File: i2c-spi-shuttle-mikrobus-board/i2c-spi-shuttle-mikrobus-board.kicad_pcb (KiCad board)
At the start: 4 copper layers, 25.4 x 42.9 mm, 14 parts, among them J1 Conn_01x08, J2 Conn_01x08, J3 Shuttle, SW1 ADDR, U1 SC18IS606PW, U2 PCAL9538APW

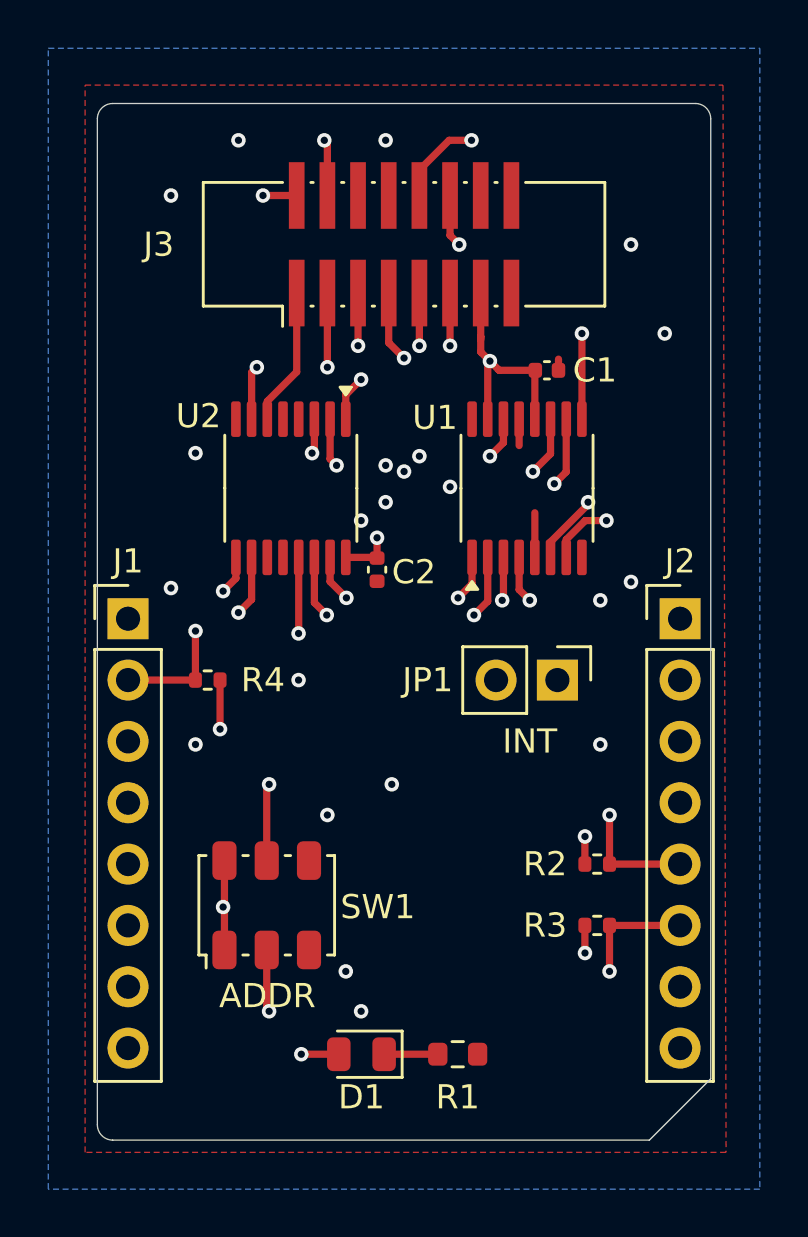
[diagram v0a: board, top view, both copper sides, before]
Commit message: fix shuttle pinout in schematic, clear PCB of tracks (we must reroute)
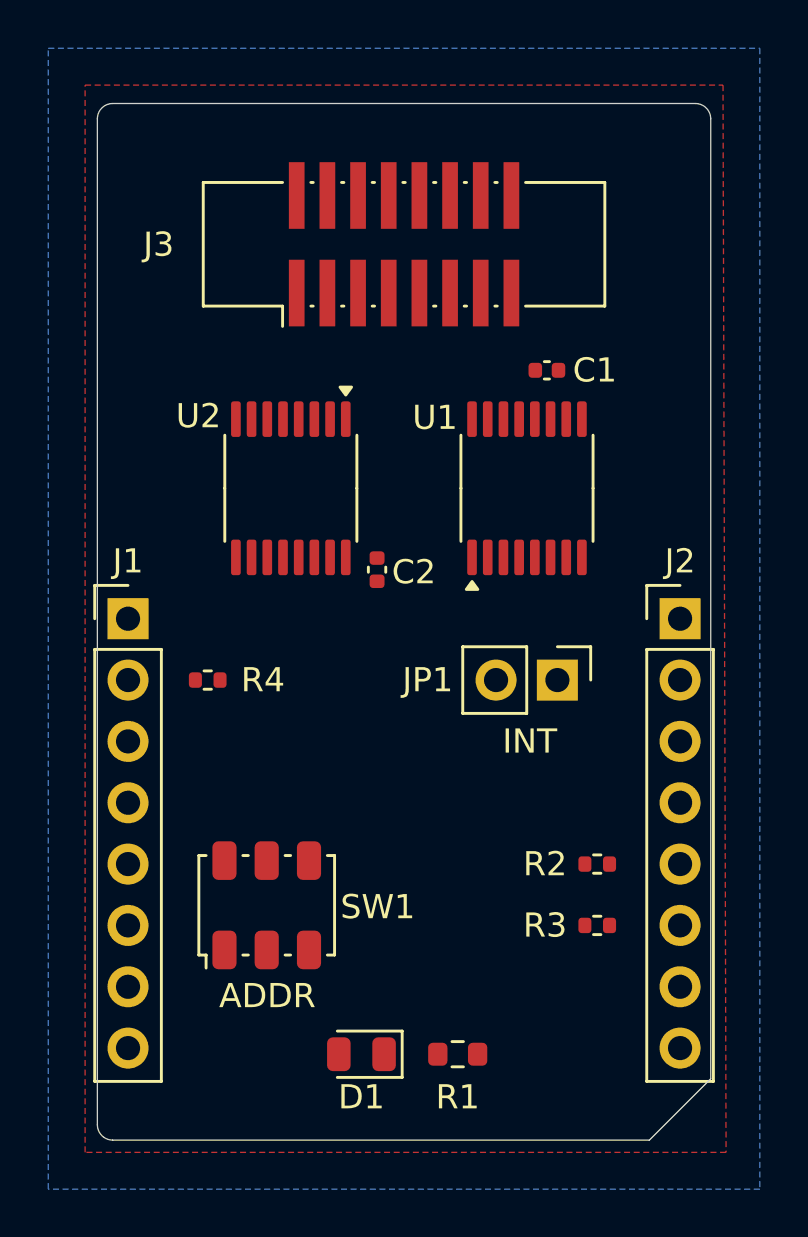
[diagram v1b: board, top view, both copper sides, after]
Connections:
- J3 pad 1: /OUT_AN -> /GND
- J3 pad 10: /SCL -> /OUT_SCK
- J3 pad 11: /OUT_COPI -> /OUT_RX
- J3 pad 12: /SDA -> /OUT_~{CS}
- J3 pad 13: /+3.3V -> /OUT_~{INT}
- J3 pad 14: /OUT_+5V -> /OUT_~{RST}
- J3 pad 15: /GND -> /OUT_PWM
- J3 pad 16: /GND -> /OUT_AN
- J3 pad 2: /OUT_PWM -> /GND
- J3 pad 3: /OUT_~{RST} -> /OUT_+5V
- J3 pad 4: /OUT_~{INT} -> /+3.3V
- J3 pad 5: /OUT_~{CS} -> /SDA
- J3 pad 6: /OUT_RX -> /OUT_COPI
- J3 pad 7: /OUT_SCK -> /SCL
- J3 pad 8: /OUT_TX -> /OUT_CIPO
- J3 pad 9: /OUT_CIPO -> /OUT_TX
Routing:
- net /SDA: track 70.4 -> 0.00 mm, vias 7 -> 0
- net /SCL: track 59.7 -> 0.00 mm, vias 5 -> 0
- net /IN_~{RST}: track 50.8 -> 0.00 mm, vias 7 -> 0
- net /A0: track 47.3 -> 0.00 mm, vias 5 -> 0
- net /A1: track 37.0 -> 0.00 mm, vias 6 -> 0
- net /OUT_~{INT}: track 28.0 -> 0.00 mm, vias 3 -> 0
- net /OUT_PWM: track 25.3 -> 0.00 mm, vias 4 -> 0
- net /+3.3V: track 22.4 -> 0.00 mm, vias 7 -> 0
- net /MID_~{INT}: track 18.5 -> 0.00 mm, vias 3 -> 0
- net /OUT_SCK: track 15.5 -> 0.00 mm, vias 3 -> 0
- net /OUT_COPI: track 15.3 -> 0.00 mm, vias 3 -> 0
- net /OUT_~{CS}: track 15.2 -> 0.00 mm, vias 2 -> 0
- net /OUT_CIPO: track 11.4 -> 0.00 mm, vias 3 -> 0
- net /OUT_~{RST}: track 8.23 -> 0.00 mm, vias 2 -> 0
- net /OUT_AN: track 5.73 -> 0.00 mm
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
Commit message: route the I2C-SPI Shuttle board now that the pinout is fixed
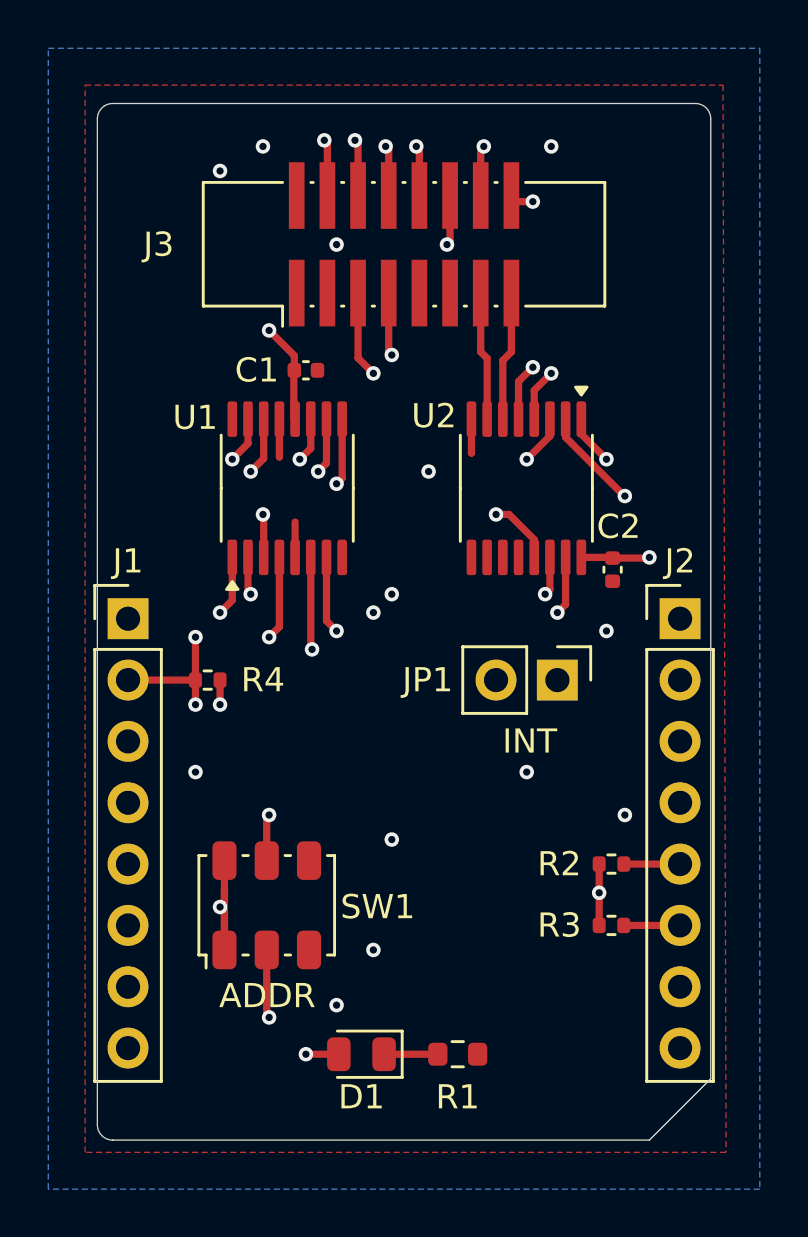
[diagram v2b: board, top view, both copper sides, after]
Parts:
- moved C1 9.98 mm to (84.8, 46.9)
- moved U1 9.93 mm to (84.1, 51.7)
- moved C2 9.75 mm to (97.5, 55.1)
- moved U2 9.75 mm to (94.0, 51.7)
- moved R2 0.59 mm to (97.5, 67.3)
- moved R3 0.59 mm to (97.5, 69.8)
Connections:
- U2 pad 10: /OUT_~{INT} -> unconnected-(U2-IO5-Pad10)
- U2 pad 4: unconnected-(U2-IO0-Pad4) -> /OUT_~{RST}
- U2 pad 5: unconnected-(U2-IO1-Pad5) -> /OUT_AN
- U2 pad 6: /OUT_AN -> /OUT_PWM
- U2 pad 7: /OUT_~{RST} -> /OUT_~{INT}
- U2 pad 9: /OUT_PWM -> unconnected-(U2-IO4-Pad9)
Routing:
- net /SDA: track 0.00 -> 61.8 mm, vias 0 -> 5
- net /SCL: track 0.00 -> 52.7 mm, vias 0 -> 5
- net /A1: track 0.00 -> 45.5 mm, vias 0 -> 4
- net /A0: track 0.00 -> 44.9 mm, vias 0 -> 5
- net /IN_~{RST}: track 0.00 -> 43.6 mm, vias 0 -> 6
- net /OUT_CIPO: track 0.00 -> 24.7 mm, vias 0 -> 3
- net /OUT_SCK: track 0.00 -> 24.7 mm, vias 0 -> 3
- net /+3.3V: track 0.00 -> 23.1 mm, vias 0 -> 9
- net /MID_~{INT}: track 0.00 -> 21.0 mm, vias 0 -> 2
- net /OUT_~{CS}: track 0.00 -> 19.3 mm, vias 0 -> 3
- net /OUT_COPI: track 0.00 -> 19.0 mm, vias 0 -> 2
- net /OUT_~{RST}: track 0.00 -> 16.5 mm, vias 0 -> 3
- net /OUT_AN: track 0.00 -> 9.89 mm, vias 0 -> 2
- net /OUT_PWM: track 0.00 -> 5.37 mm
- net /OUT_~{INT}: track 0.00 -> 5.33 mm
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
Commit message: annotate schematic & board, pass +5V, update constraints
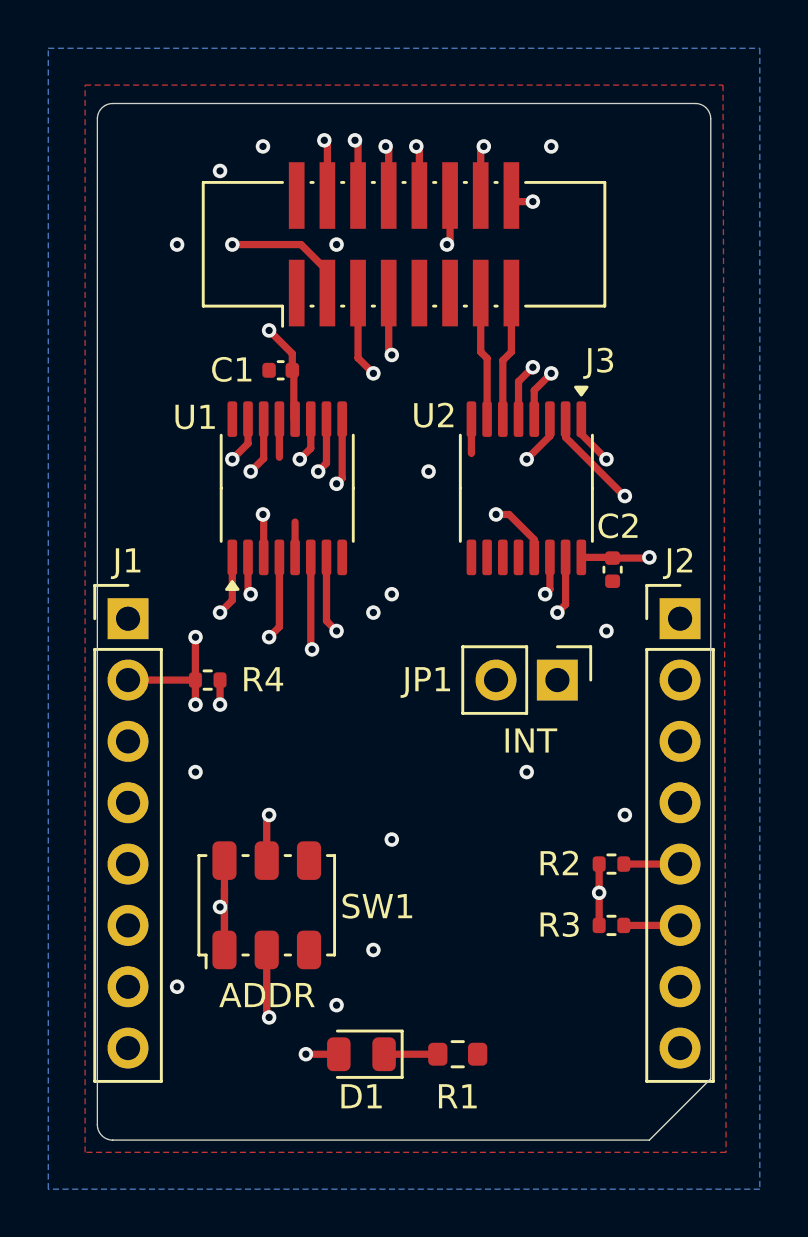
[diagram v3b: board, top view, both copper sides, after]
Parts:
- moved C1 1.04 mm to (83.8, 46.9), turned to 180 degrees
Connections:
- J2 pad 7: /IN_+5V -> /+5V
- J3 pad 3: /OUT_+5V -> /+5V
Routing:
- net /+5V: track 0.00 -> 59.2 mm, vias 0 -> 3
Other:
- board text added: "+3.3V"
- board text added: "+5V"
- board text added: "AN"
- board text added: "CIPO"
- board text added: "COPI"
- board text added: "CS"
- board text added: "GND"
- board text added: "INT"
- board text added: "I^{2}C to SPI shuttle board"
- board text added: "NC"
- board text added: "PWM"
- board text added: "RST"
- board text added: "RX"
- board text added: "SCK"
- board text added: "SCL"
- board text added: "SDA"
- board text added: "TX"
- board text added: "independent, I^{2}C GPIO"
- board text added: "independent, I^{2}C ↔ SPI"
- board text added: "not passed"
- board text added: "passed 1:1"
- board text added: "~{INT}"
- board text added: "~{RST}"

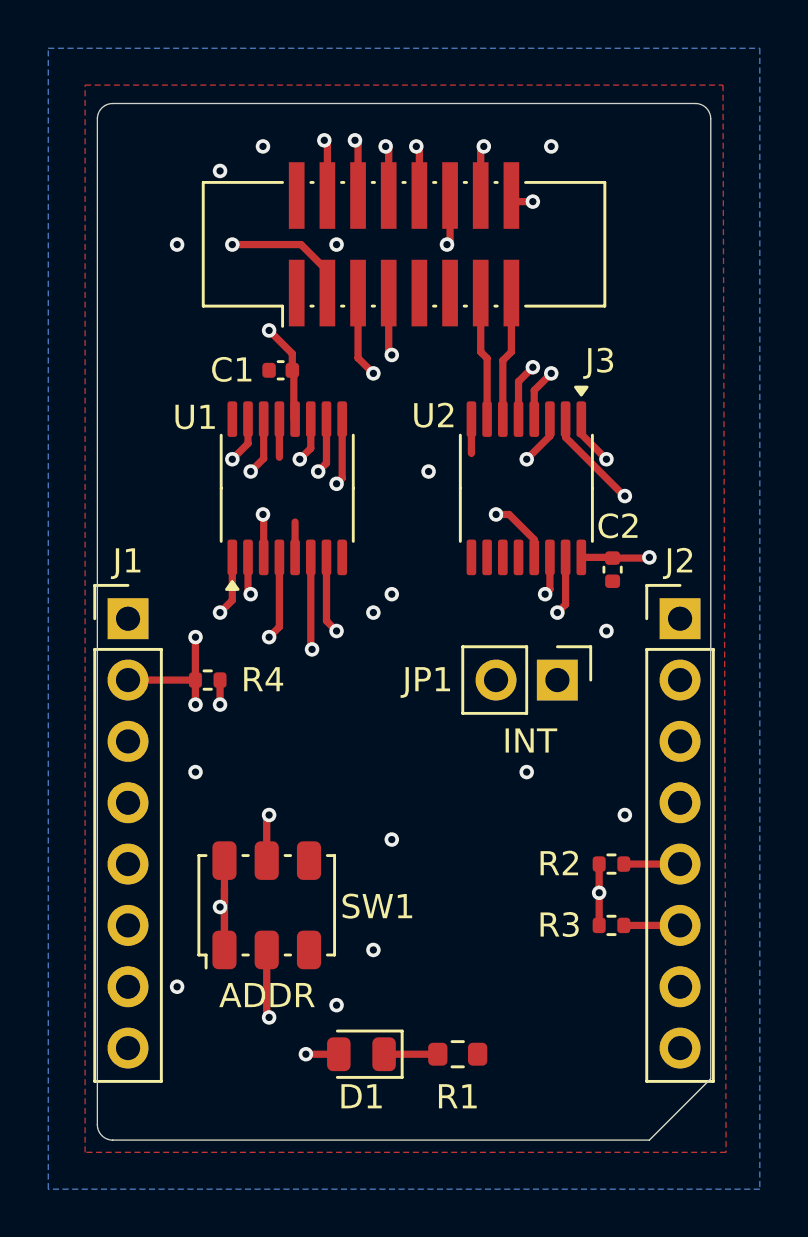
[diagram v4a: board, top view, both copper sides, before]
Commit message: i2c spi shuttle: add mounting holes, JLC number placeholder, front label
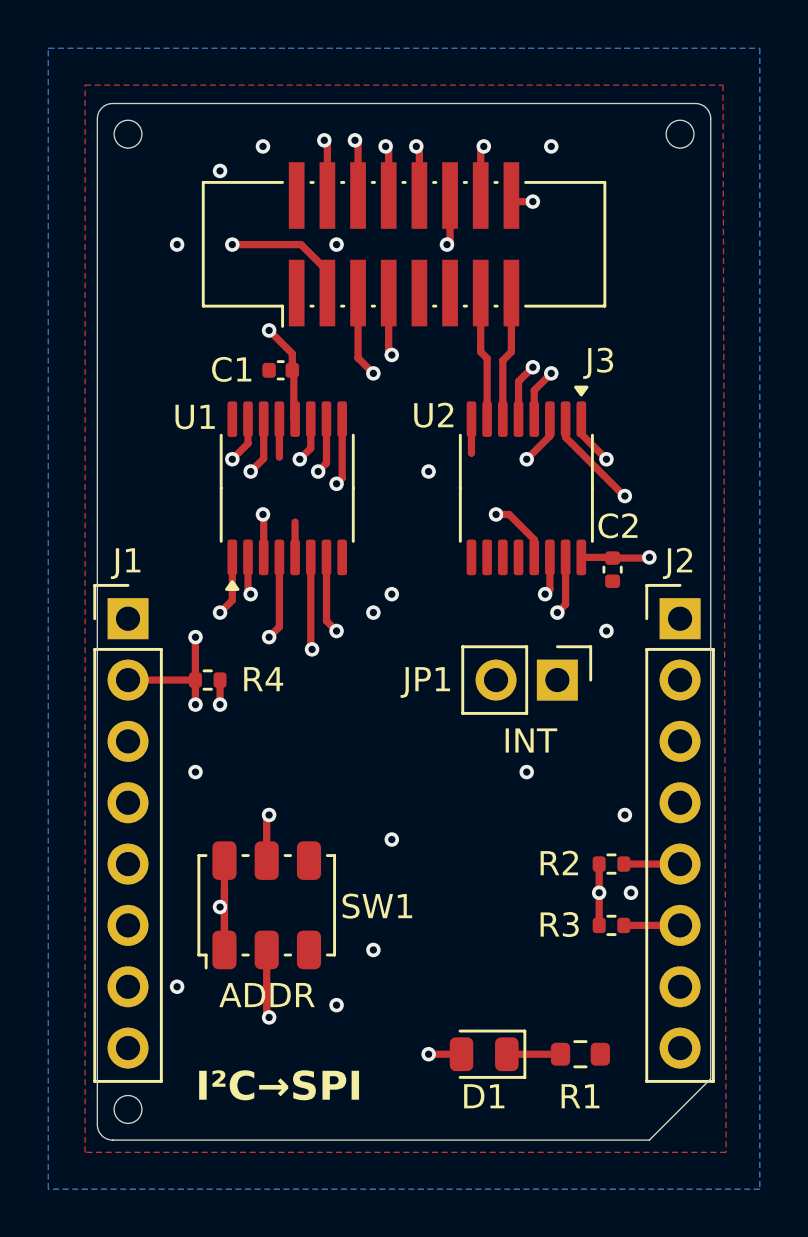
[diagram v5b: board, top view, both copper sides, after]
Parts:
- added REF**: ToolingHole_1.152mm, MountingHole:ToolingHole_1.152mm, F.Cu at (77.5, 37.1)
- added REF**: ToolingHole_1.152mm, MountingHole:ToolingHole_1.152mm, F.Cu at (100.3, 37.1)
- added REF**: ToolingHole_1.152mm, MountingHole:ToolingHole_1.152mm, F.Cu at (77.5, 77.5)
- moved D1 5.08 mm to (92.2, 75.2)
- moved R1 5.08 mm to (96.2, 75.2)
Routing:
- net /GND: vias 0 -> 1
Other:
- board text added: "I²C→SPI"
- board text added: "JLCJLCJLCJLC"
